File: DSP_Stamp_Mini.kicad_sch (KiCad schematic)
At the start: 68 parts, among them J1 Conn_01x10, J2 SM03B-SRSS-TB, J3 Conn_01x04, J4 USB_C_Receptacle_USB2.0_14P, J5 Conn_01x04, J6 Conn_01x10, J7 Conn_01x02, J8 Conn_01x04, SW1 SW_Push, SW2 SW_Push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

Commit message: small schematic changes for readability
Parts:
- added C26, C27, C28: 100n, Capacitor_SMD:C_0603_1608Metric_Pad1.08x0.95mm_HandSolder, symbol Device:C
- added C29, C30: 10u, Capacitor_SMD:C_0603_1608Metric_Pad1.08x0.95mm_HandSolder, symbol Device:C
- added U5: AZ1117-3.3, symbol Regulator_Linear:AZ1117-3.3
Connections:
- net +3V3: now also C27.1, C29.1, U5.2 (VO); no longer J7.1 (Pin_1)
- net +5V: now also J7.1 (Pin_1), C26.1, C28.1, C30.1, U5.3 (VI)
- net GND: now also C26.2, C27.2, C28.2, C29.2, C30.2, U5.1 (GND)
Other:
- note added: "VCOM can be used to bias the in<->out op amps"

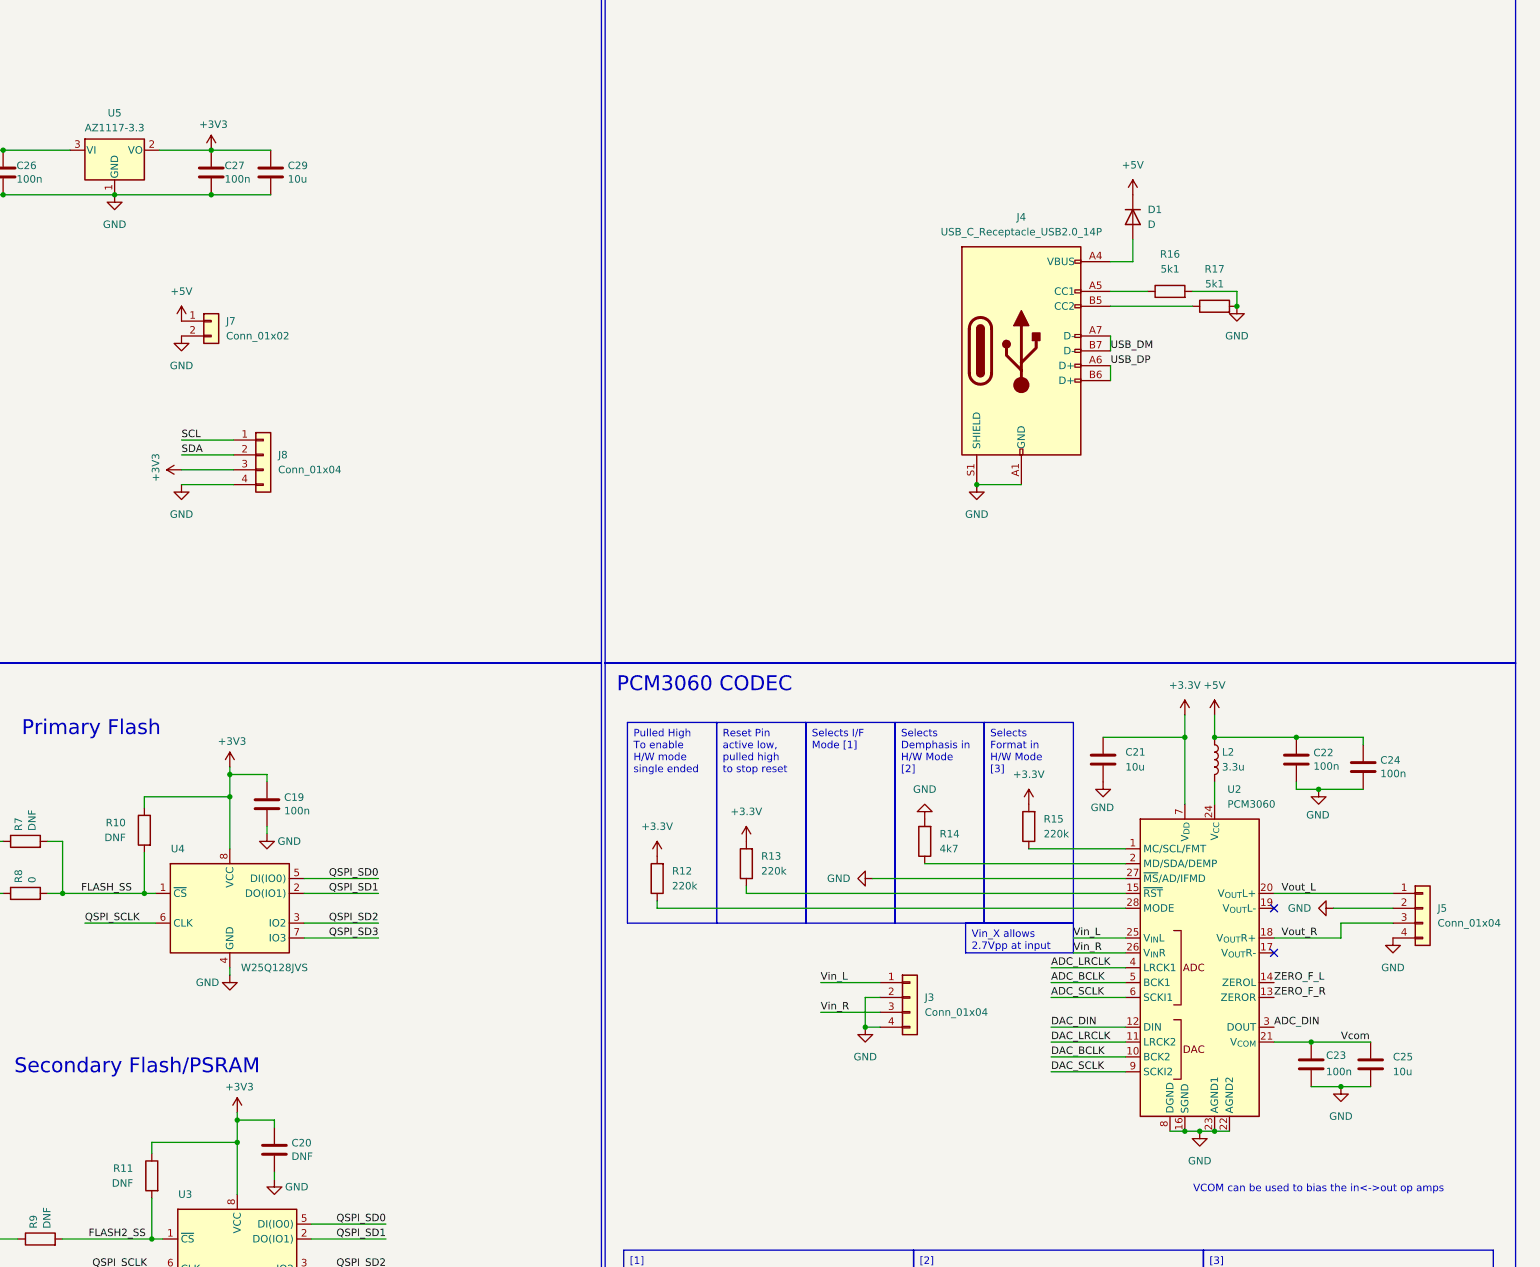
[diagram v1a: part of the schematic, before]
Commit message: switched pin headers to SMD, changed board shape and redid layout
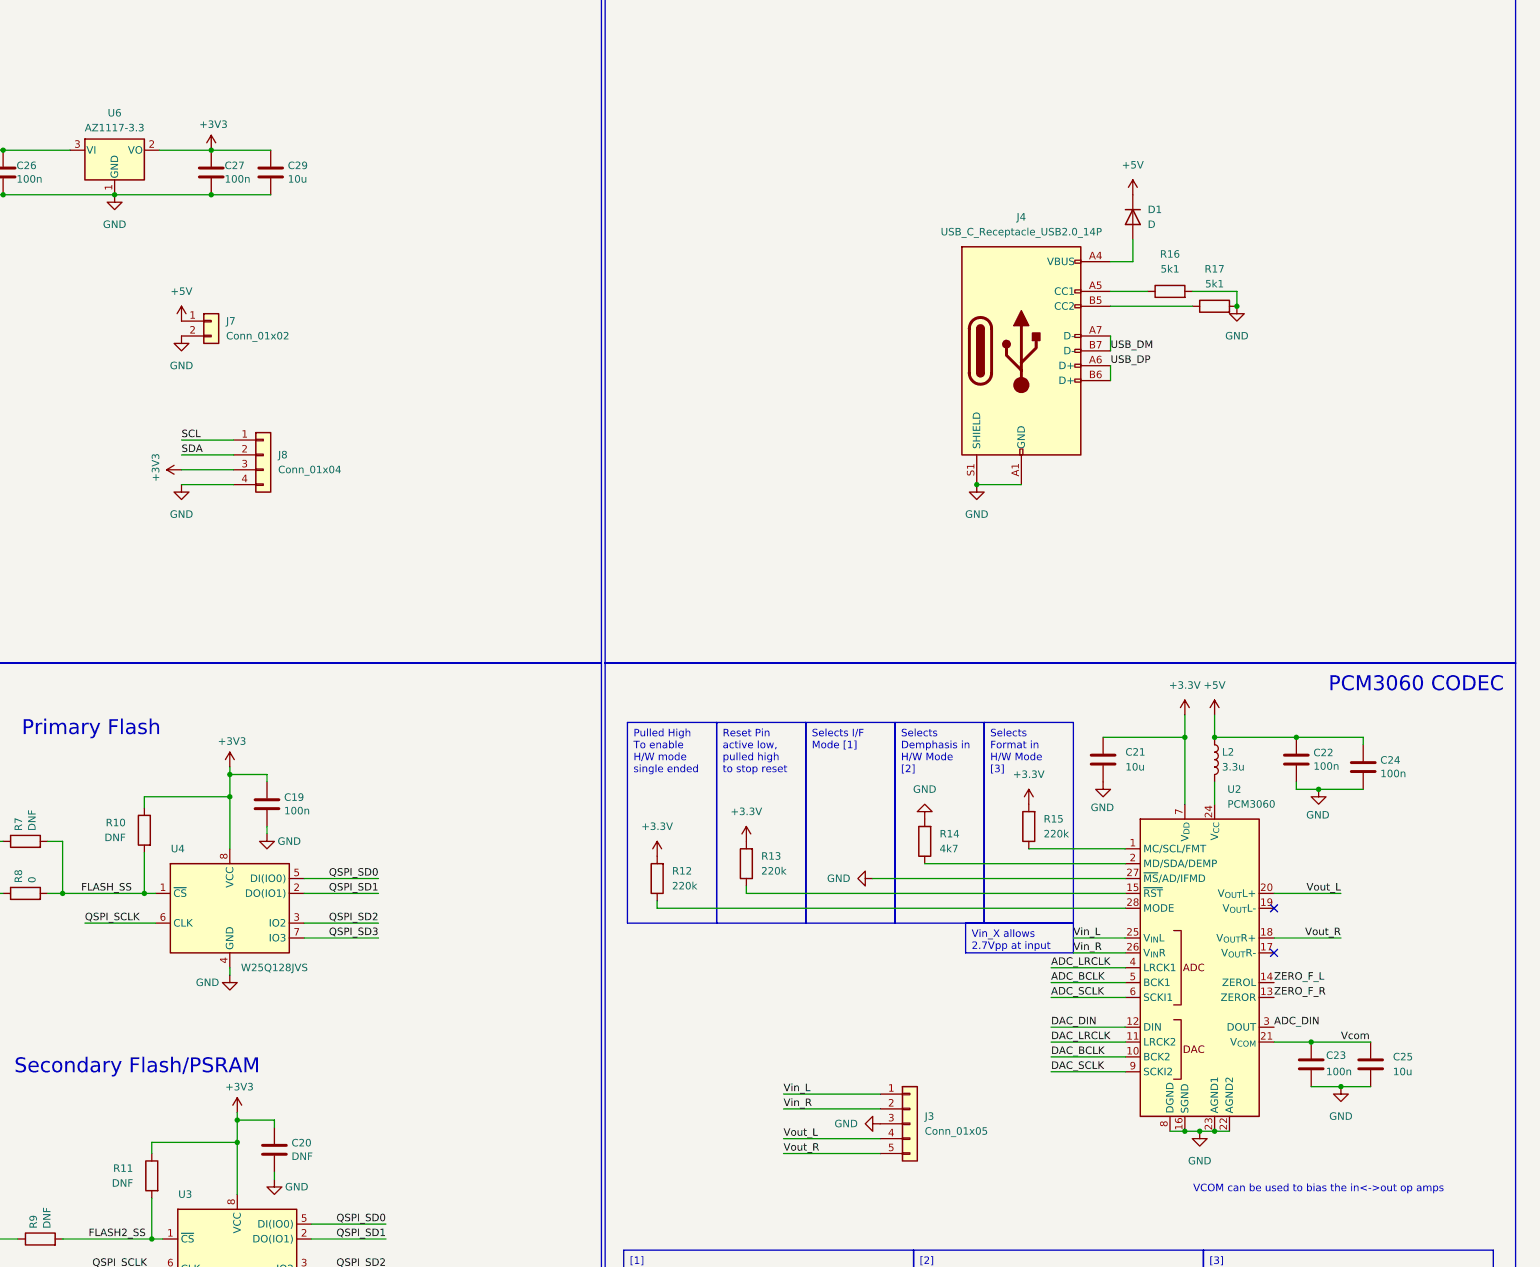
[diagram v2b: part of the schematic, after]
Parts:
- removed J3, J5: Conn_01x04, Connector_PinHeader_2.54mm:PinHeader_1x04_P2.54mm_Vertical, symbol Connector_Generic:Conn_01x04
- removed U5: AZ1117-3.3, symbol Regulator_Linear:AZ1117-3.3
- added J3: Conn_01x05, Connector_PinHeader_2.54mm:PinHeader_1x05_P2.54mm_Vertical_SMD_Pin1Right, symbol Connector_Generic:Conn_01x05
- added U6: AZ1117-3.3, Package_TO_SOT_SMD:SOT-89-3, symbol Regulator_Linear:AZ1117-3.3
- J1, J6: footprint Connector_PinHeader_2.54mm:PinHeader_1x10_P2.54mm_Vertical -> Connector_PinHeader_2.54mm:PinHeader_1x10_P2.54mm_Vertical_SMD_Pin1Right
- J7: footprint 4ms_Connector:Pins_1x02_2.54mm_TH -> Connector_PinHeader_2.54mm:PinHeader_1x02_P2.54mm_Vertical_SMD_Pin1Right
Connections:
- net +3V3: now also U6.2 (VO)
- net +5V: now also U6.3 (VI)
- net GND: now also J3.3 (Pin_3), U6.1 (GND)
- net Vin_L: now also J3.1 (Pin_1)
- net Vin_R: now also J3.2 (Pin_2)
- net Vout_L: now also J3.4 (Pin_4)
- net Vout_R: now also J3.5 (Pin_5)
